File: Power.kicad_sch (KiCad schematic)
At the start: 3 parts, among them U3 TLV75533PDRV

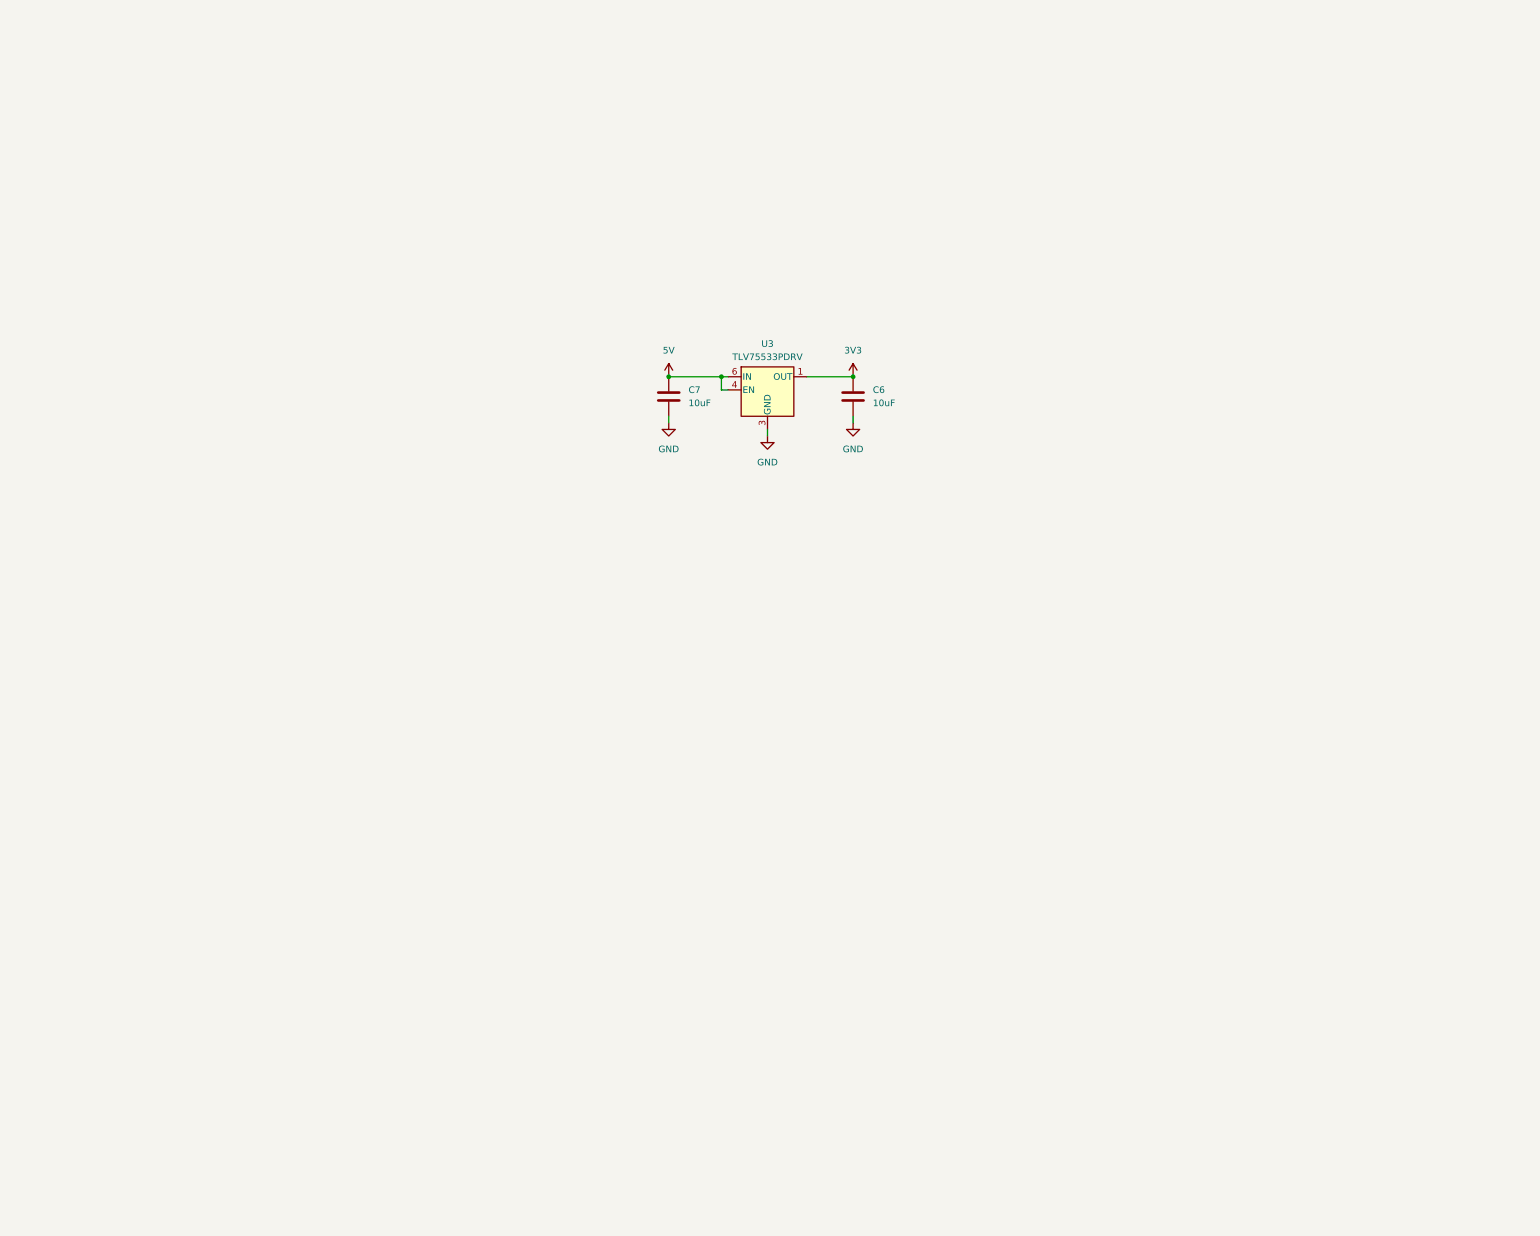
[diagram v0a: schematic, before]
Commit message: add power supplies
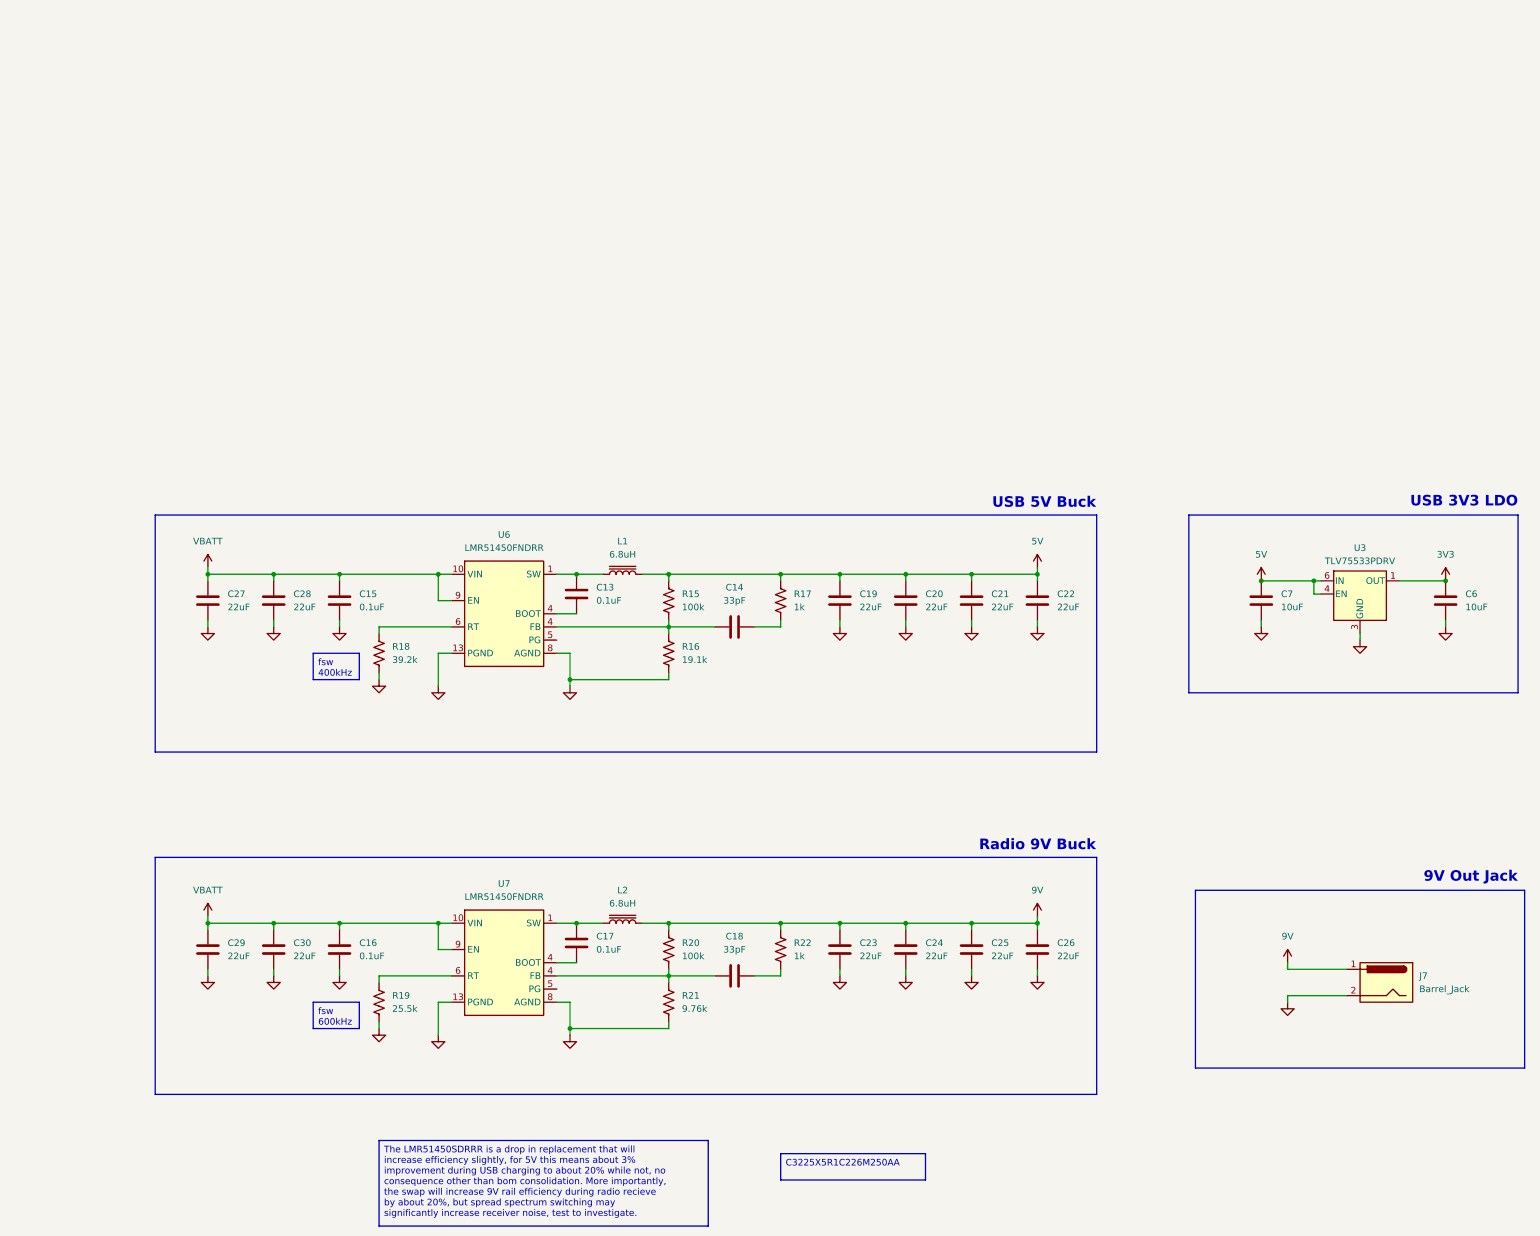
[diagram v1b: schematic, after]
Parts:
- added C13, C15, C16, C17: 0.1uF, symbol Cave_Radio_PDB:0.1uF
- added C14, C18: 33pF, symbol Cave_Radio_PDB:33pF
- added C19, C20, C21, C22, C23, C24, C25, C26, C27, C28, C29, C30: 22uF, symbol Cave_Radio_PDB:22uF
- added J7: Barrel_Jack, symbol Cave_Radio_PDB:Barrel_Jack
- added L1, L2: 6.8uH, symbol Cave_Radio_PDB:6.8uH
- added R15, R20: 100k, symbol Cave_Radio_PDB:100k
- added R16: 19.1k, symbol Cave_Radio_PDB:19.1k
- added R17, R22: 1k, symbol Cave_Radio_PDB:1k
- added R18: 39.2k, symbol Cave_Radio_PDB:39.2k
- added R19: 25.5k, symbol Cave_Radio_PDB:25.5k
- added R21: 9.76k, symbol Cave_Radio_PDB:9.76k
- added U6, U7: LMR51450FNDRR, Cave_Radio_PDB:WSON-12-1EP_3x3mm_P0.5mm_EP1.5x2.5mm_ThermalVias, symbol Cave_Radio_PDB:LMR51450FNDRR
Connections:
- net 5V: now also C19.1, C20.1, C21.1, C22.1, L1.2, R15.1, R17.1
- net GND: now also C15.2, C16.2, C19.2, C20.2, C21.2, C22.2, C23.2, C24.2, C25.2, C26.2, C27.2, C28.2, C29.2, C30.2, J7.2, R16.2, R18.2, R19.2, R21.2, U6.13 (PGND), U6.8 (AGND), U7.13 (PGND), U7.8 (AGND)
- new net: C13.1, L1.1, U6.1 (SW), U6.2 (SW), U6.3 (SW)
- new net: C13.2, U6.4 (FB)
- new net: C14.1, R15.2, R16.1, U6.4 (FB)
- new net: R18.1, U6.6 (RT)
- new net: C17.1, L2.1, U7.1 (SW), U7.2 (SW), U7.3 (SW)
- new net: C17.2, U7.4 (FB)
- new net: C18.2, R22.2
- new net: C18.1, R20.2, R21.1, U7.4 (FB)
- new net: C14.2, R17.2
- new net: R19.1, U7.6 (RT)
- new net 9V: C23.1, C24.1, C25.1, C26.1, J7.1, L2.2, R20.1, R22.1
- new net VBATT: C15.1, C16.1, C27.1, C28.1, C29.1, C30.1, U6.10 (VIN), U6.11 (VIN), U6.12 (VIN), U6.9 (EN), U7.10 (VIN), U7.11 (VIN), U7.12 (VIN), U7.9 (EN)
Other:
- note added: "9V Out Jack"
- note added: "Radio 9V Buck"
- note added: "USB 3V3 LDO"
- note added: "USB 5V Buck"
- moved on the sheet: C6, C7, U3

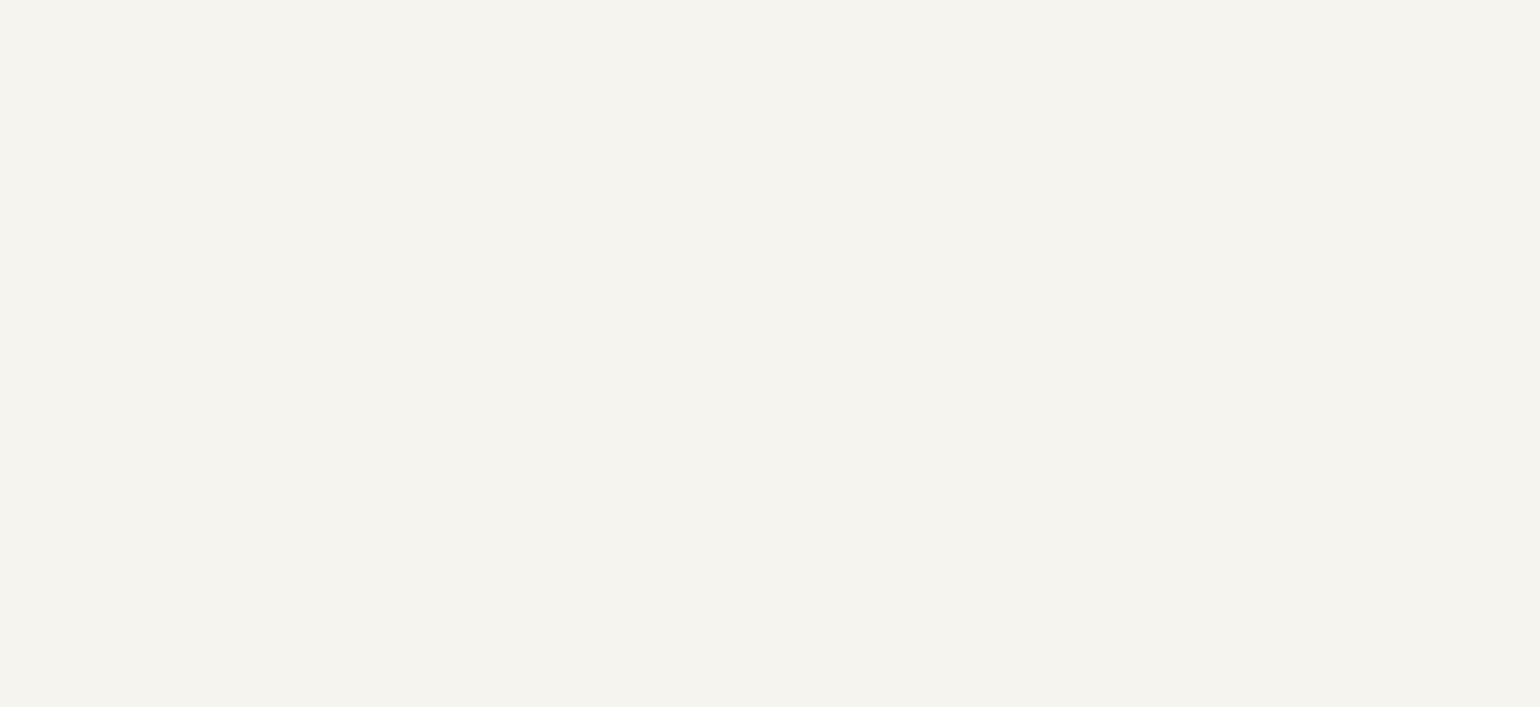
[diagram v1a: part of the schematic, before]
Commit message: start efuse and rough layout
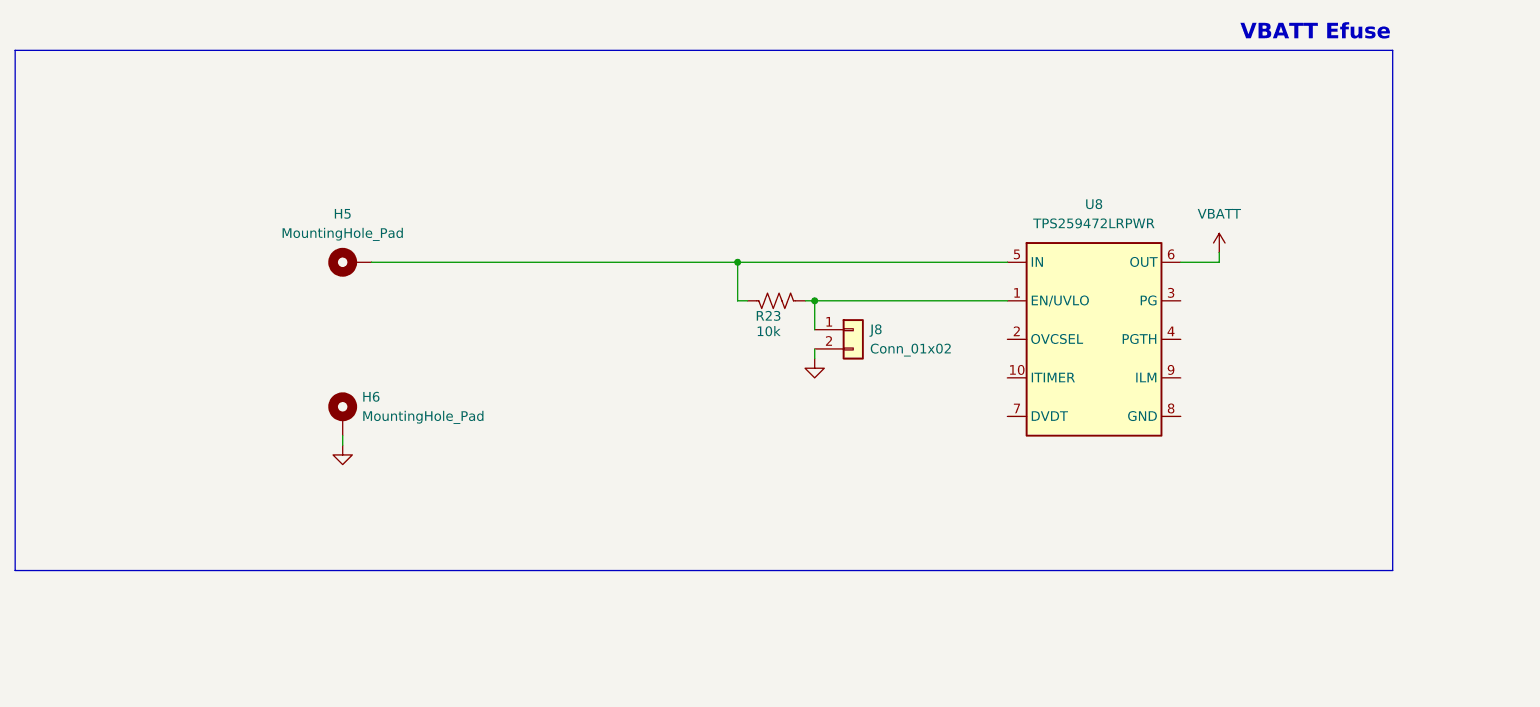
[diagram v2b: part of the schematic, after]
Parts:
- added H5, H6: MountingHole_Pad, Cave_Radio_PDB:MountingHole_3.2mm_M3_DIN965_Pad_TopBottom, symbol Cave_Radio_PDB:MountingHole_Pad
- added J8: Conn_01x02, Cave_Radio_PDB:CONN_TSW-102-S_SAI, symbol Cave_Radio_PDB:Conn_01x02
- added R23: 10k, Cave_Radio_PDB:R_0402_1005Metric, symbol Cave_Radio_PDB:10k
- added U8: TPS259472LRPWR, Package_SON:VSON-10-1EP_3x3mm_P0.5mm_EP1.65x2.4mm_ThermalVias, symbol Cave_Radio_PDB:TPS259472LRPWR
- C13, C14, C15, C16, C17, C18, C6, C7: footprint (none) -> Cave_Radio_PDB:C_0402_1005Metric
- C19, C20, C21, C22, C23, C24, C25, C26, C27, C28, C29, C30: footprint (none) -> Cave_Radio_PDB:CAP_C3225X5R1C226M250AA
- J7: footprint (none) -> Cave_Radio_PDB:CUI_PJ-102A
- L1, L2: footprint (none) -> Cave_Radio_PDB:IND_SPR5050_BRN-M
- R15, R16, R17, R18, R19, R20, R21, R22: footprint (none) -> Cave_Radio_PDB:R_0402_1005Metric
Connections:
- net GND: now also H6.1, J8.2 (Pin_2)
- net VBATT: now also U8.6 (OUT)
- new net: H5.1, R23.1, U8.5 (IN)
- new net: J8.1 (Pin_1), R23.2, U8.1 (EN/UVLO)
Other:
- note added: "VBATT Efuse"
